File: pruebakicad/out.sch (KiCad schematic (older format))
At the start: 7 parts, among them J1 Conn_2Rows-07Pins_MountingPin, J2 Conn_01x04_MountingPin, J3 Conn_01x03, J4 Conn_2Rows-15Pins

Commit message: uart_added
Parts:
- added C6: 0.1uF, symbol Device:C_Small
- added J5: Conn_01x04, symbol Elementos:Conn_01x04
- renumbered R5 to R10, R6 to R11
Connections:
- net +3V3: now also C6.1, J5.1 (VCC)
- net GND: now also C6.2, J5.4 (GND)
- new net RXD0: J5.3 (RXD0)
- new net TXD0: J5.2 (TXD0)
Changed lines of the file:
@@
 $Descr A4 11693 8268
 encoding utf-8
-Sheet 2 3
+Sheet 2 4
 Title ""
 Date ""
@@
 $EndComp
 $Comp
-L Device:R_Small_US R5
+L Device:R_Small_US R10
 U 1 1 60810B34
 P 4050 4450
-F 0 "R5" H 4118 4496 50  0000 L CNN
+F 0 "R10" H 4118 4496 50  0000 L CNN
 F 1 "10k" H 4118 4405 50  0000 L CNN
 F 2 "" H 4050 4450 50  0001 C CNN
@@
 	4050 4700 4050 4800
 $Comp
-L Device:R_Small_US R6
+L Device:R_Small_US R11
 U 1 1 60810B54
 P 4050 4900
-F 0 "R6" H 4118 4946 50  0000 L CNN
+F 0 "R11" H 4118 4946 50  0000 L CNN
 F 1 "10k" H 4118 4855 50  0000 L CNN
 F 2 "" H 4050 4900 50  0001 C CNN
@@
 Wire Wire Line
 	6550 3650 6350 3650
+$Comp
+L Elementos:Conn_01x04 J?
+U 1 1 608DA23F
+P 7400 4750
+AR Path="/6077B277/608DA23F" Ref="J?"  Part="1"
+AR Path="/6080574C/608DA23F" Ref="J5"  Part="1"
+F 0 "J5" H 7480 4742 50  0000 L CNN
+F 1 "Conn_01x04" H 7480 4651 50  0000 L CNN
+F 2 "" H 7400 4750 50  0001 C CNN
+F 3 "~" H 7400 4750 50  0001 C CNN
+	1    7400 4750
+	1    0    0    -1
+$EndComp
+$Comp
+L Device:C_Small C?
+U 1 1 608DA247
+P 6750 4800
+AR Path="/6077B277/608DA247" Ref="C?"  Part="1"
+AR Path="/6080574C/608DA247" Ref="C6"  Part="1"
+F 0 "C6" H 6550 4850 50  0000 L CNN
+F 1 "0.1uF" H 6450 4750 50  0000 L CNN
+F 2 "" H 6750 4800 50  0001 C CNN
+F 3 "~" H 6750 4800 50  0001 C CNN
+	1    6750 4800
+	1    0    0    -1
+$EndComp
+$Comp
+L power:+3.3V #PWR?
+U 1 1 608DA251
+P 6750 4500
+AR Path="/6077B277/608DA251" Ref="#PWR?"  Part="1"
+AR Path="/6080574C/608DA251" Ref="#PWR?"  Part="1"
+F 0 "#PWR?" H 6750 4350 50  0001 C CNN
+F 1 "+3.3V" H 6765 4673 50  0000 C CNN
+F 2 "" H 6750 4500 50  0001 C CNN
+F 3 "" H 6750 4500 50  0001 C CNN
+	1    6750 4500
+	1    0    0    -1
+$EndComp
+$Comp
+L power:GND #PWR?
+U 1 1 608DA257
+P 6750 5050
+AR Path="/6077B277/608DA257" Ref="#PWR?"  Part="1"
+AR Path="/6080574C/608DA257" Ref="#PWR?"  Part="1"
+F 0 "#PWR?" H 6750 4800 50  0001 C CNN
+F 1 "GND" H 6755 4877 50  0000 C CNN
+F 2 "" H 6750 5050 50  0001 C CNN
+F 3 "" H 6750 5050 50  0001 C CNN
+	1    6750 5050
+	1    0    0    -1
+$EndComp
+Text HLabel 7100 4750 0    50   Input ~ 0
+TXD0
+Text HLabel 7100 4850 0    50   Input ~ 0
+RXD0
+Wire Wire Line
+	7200 4750 7100 4750
+Wire Wire Line
+	7200 4850 7100 4850
+Wire Wire Line
+	6750 4500 6750 4650
+Wire Wire Line
+	6750 4900 6750 4950
+Wire Wire Line
+	7200 4650 6750 4650
+Connection ~ 6750 4650
+Wire Wire Line
+	6750 4650 6750 4700
+Wire Wire Line
+	7200 4950 6750 4950
+Connection ~ 6750 4950
+Wire Wire Line
+	6750 4950 6750 5050
 $EndSCHEMATC

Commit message: footprints
Footprints added
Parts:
- BZ1: footprint (none) -> Buzzer_Beeper:Buzzer_12x9.5RM7.6
- C6: footprint (none) -> Capacitor_SMD:C_0805_2012Metric
- J1: value Conn_2Rows-07Pins_MountingPin -> Conn_01x08_RC522; footprint (none) -> Connector_PinHeader_1.00mm:PinHeader_1x08_P1.00mm_Vertical
- J2, J5: footprint (none) -> Connector_PinHeader_1.00mm:PinHeader_1x04_P1.00mm_Vertical
- J3: footprint (none) -> Connector_PinHeader_1.00mm:PinHeader_1x03_P1.00mm_Vertical
- J4: footprint (none) -> Connector_PinHeader_1.00mm:PinHeader_2x15_P1.00mm_Vertical
- R10, R11: footprint (none) -> Resistor_SMD:R_0805_2012Metric
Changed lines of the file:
@@
 $EndDescr
 $Comp
-L power:+3V3 #PWR?
+L power:+3V3 #PWR0101
 U 1 1 60810B15
 P 4300 3700
-F 0 "#PWR?" H 4300 3550 50  0001 C CNN
+F 0 "#PWR0101" H 4300 3550 50  0001 C CNN
 F 1 "+3V3" H 4315 3873 50  0000 C CNN
 F 2 "" H 4300 3700 50  0001 C CNN
@@
 $EndComp
 $Comp
-L power:GND #PWR?
+L power:GND #PWR0102
 U 1 1 60810B1D
 P 4000 3500
-F 0 "#PWR?" H 4000 3250 50  0001 C CNN
+F 0 "#PWR0102" H 4000 3250 50  0001 C CNN
 F 1 "GND" H 4005 3327 50  0000 C CNN
 F 2 "" H 4000 3500 50  0001 C CNN
@@
 	4550 4800 4300 4800
 $Comp
-L power:GND #PWR?
+L power:GND #PWR0103
 U 1 1 60810B26
 P 4300 4950
-F 0 "#PWR?" H 4300 4700 50  0001 C CNN
+F 0 "#PWR0103" H 4300 4700 50  0001 C CNN
 F 1 "GND" H 4305 4777 50  0000 C CNN
 F 2 "" H 4300 4950 50  0001 C CNN
@@
 	4300 4800 4300 4950
 $Comp
-L power:+5V #PWR?
+L power:+5V #PWR0104
 U 1 1 60810B2E
 P 4300 4400
-F 0 "#PWR?" H 4300 4250 50  0001 C CNN
+F 0 "#PWR0104" H 4300 4250 50  0001 C CNN
 F 1 "+5V" H 4315 4573 50  0000 C CNN
 F 2 "" H 4300 4400 50  0001 C CNN
@@
 F 0 "R10" H 4118 4496 50  0000 L CNN
 F 1 "10k" H 4118 4405 50  0000 L CNN
-F 2 "" H 4050 4450 50  0001 C CNN
+F 2 "Resistor_SMD:R_0805_2012Metric" H 4050 4450 50  0001 C CNN
 F 3 "~" H 4050 4450 50  0001 C CNN
 	1    4050 4450
@@
 	4050 4350 4050 4250
 $Comp
-L power:+5V #PWR?
+L power:+5V #PWR0105
 U 1 1 60810B3F
 P 4050 4250
-F 0 "#PWR?" H 4050 4100 50  0001 C CNN
+F 0 "#PWR0105" H 4050 4100 50  0001 C CNN
 F 1 "+5V" H 4065 4423 50  0000 C CNN
 F 2 "" H 4050 4250 50  0001 C CNN
@@
 F 0 "J2" H 4838 4514 50  0000 L CNN
 F 1 "Conn_01x04_MountingPin" H 4838 4423 50  0000 L CNN
-F 2 "" H 4750 4600 50  0001 C CNN
+F 2 "Connector_PinHeader_1.00mm:PinHeader_1x04_P1.00mm_Vertical" H 4750 4600 50  0001 C CNN
 F 3 "~" H 4750 4600 50  0001 C CNN
 	1    4750 4600
@@
 $EndComp
 $Comp
-L power:+5V #PWR?
+L power:+5V #PWR0106
 U 1 1 60810B4B
 P 4050 5100
-F 0 "#PWR?" H 4050 4950 50  0001 C CNN
+F 0 "#PWR0106" H 4050 4950 50  0001 C CNN
 F 1 "+5V" H 4065 5273 50  0000 C CNN
 F 2 "" H 4050 5100 50  0001 C CNN
@@
 F 0 "R11" H 4118 4946 50  0000 L CNN
 F 1 "10k" H 4118 4855 50  0000 L CNN
-F 2 "" H 4050 4900 50  0001 C CNN
+F 2 "Resistor_SMD:R_0805_2012Metric" H 4050 4900 50  0001 C CNN
 F 3 "~" H 4050 4900 50  0001 C CNN
 	1    4050 4900
@@
 F 0 "BZ1" H 4702 2279 50  0000 L CNN
 F 1 "Buzzer" H 4702 2188 50  0000 L CNN
-F 2 "" V 4525 2350 50  0001 C CNN
+F 2 "Buzzer_Beeper:Buzzer_12x9.5RM7.6" V 4525 2350 50  0001 C CNN
 F 3 "~" V 4525 2350 50  0001 C CNN
 	1    4550 2250
@@
 $EndComp
 $Comp
-L power:GND #PWR?
+L power:GND #PWR0107
 U 1 1 60810B6A
 P 4450 2500
-F 0 "#PWR?" H 4450 2250 50  0001 C CNN
+F 0 "#PWR0107" H 4450 2250 50  0001 C CNN
 F 1 "GND" H 4455 2327 50  0000 C CNN
 F 2 "" H 4450 2500 50  0001 C CNN
@@
 F 0 "J3" H 4830 5642 50  0000 L CNN
 F 1 "Conn_01x03" H 4830 5551 50  0000 L CNN
-F 2 "" H 4750 5600 50  0001 C CNN
+F 2 "Connector_PinHeader_1.00mm:PinHeader_1x03_P1.00mm_Vertical" H 4750 5600 50  0001 C CNN
 F 3 "~" H 4750 5600 50  0001 C CNN
 	1    4750 5600
@@
 	4550 5700 4350 5700
 $Comp
-L power:GND #PWR?
+L power:GND #PWR0108
 U 1 1 60810B7C
 P 4150 5650
-F 0 "#PWR?" H 4150 5400 50  0001 C CNN
+F 0 "#PWR0108" H 4150 5400 50  0001 C CNN
 F 1 "GND" H 4155 5477 50  0000 C CNN
 F 2 "" H 4150 5650 50  0001 C CNN
@@
 $EndComp
 $Comp
-L power:+5V #PWR?
+L power:+5V #PWR0109
 U 1 1 60810B82
 P 4350 5800
-F 0 "#PWR?" H 4350 5650 50  0001 C CNN
+F 0 "#PWR0109" H 4350 5650 50  0001 C CNN
 F 1 "+5V" H 4365 5973 50  0000 C CNN
 F 2 "" H 4350 5800 50  0001 C CNN
@@
 AR Path="/6080574C/60810B0A" Ref="J1"  Part="1"
 F 0 "J1" H 4750 3800 50  0000 C CNN
-F 1 "Conn_2Rows-07Pins_MountingPin" H 4750 3700 50  0000 C CNN
-F 2 "" H 4750 3300 50  0001 C CNN
+F 1 "Conn_01x08_RC522" H 4750 3700 50  0000 C CNN
+F 2 "Connector_PinHeader_1.00mm:PinHeader_1x08_P1.00mm_Vertical" H 4750 3300 50  0001 C CNN
 F 3 "~" H 4750 3300 50  0001 C CNN
 	1    4750 3300
@@
 F 0 "J4" H 6850 3967 50  0000 C CNN
 F 1 "Conn_2Rows-15Pins" H 6850 3876 50  0000 C CNN
-F 2 "" H 6800 3350 50  0001 C CNN
+F 2 "Connector_PinHeader_1.00mm:PinHeader_2x15_P1.00mm_Vertical" H 6800 3350 50  0001 C CNN
 F 3 "~" H 6800 3350 50  0001 C CNN
 	1    6800 3350
@@
 	6350 3650 6350 3700
 $Comp
-L power:GND #PWR?
+L power:GND #PWR0110
 U 1 1 60833C66
 P 6350 3700
-F 0 "#PWR?" H 6350 3450 50  0001 C CNN
+F 0 "#PWR0110" H 6350 3450 50  0001 C CNN
 F 1 "GND" H 6355 3527 50  0000 C CNN
 F 2 "" H 6350 3700 50  0001 C CNN
@@
 $EndComp
 $Comp
-L power:+3.3V #PWR?
+L power:+3.3V #PWR0111
 U 1 1 608343FF
 P 6350 2850
-F 0 "#PWR?" H 6350 2700 50  0001 C CNN
+F 0 "#PWR0111" H 6350 2700 50  0001 C CNN
 F 1 "+3.3V" H 6365 3023 50  0000 C CNN
 F 2 "" H 6350 2850 50  0001 C CNN
@@
 	7100 3650 7300 3650
 $Comp
-L power:+5V #PWR?
+L power:+5V #PWR0112
 U 1 1 6083FA93
 P 7300 3650
-F 0 "#PWR?" H 7300 3500 50  0001 C CNN
+F 0 "#PWR0112" H 7300 3500 50  0001 C CNN
 F 1 "+5V" H 7315 3823 50  0000 C CNN
 F 2 "" H 7300 3650 50  0001 C CNN
@@
 F 0 "J5" H 7480 4742 50  0000 L CNN
 F 1 "Conn_01x04" H 7480 4651 50  0000 L CNN
-F 2 "" H 7400 4750 50  0001 C CNN
+F 2 "Connector_PinHeader_1.00mm:PinHeader_1x04_P1.00mm_Vertical" H 7400 4750 50  0001 C CNN
 F 3 "~" H 7400 4750 50  0001 C CNN
 	1    7400 4750
@@
 F 0 "C6" H 6550 4850 50  0000 L CNN
 F 1 "0.1uF" H 6450 4750 50  0000 L CNN
-F 2 "" H 6750 4800 50  0001 C CNN
+F 2 "Capacitor_SMD:C_0805_2012Metric" H 6750 4800 50  0001 C CNN
 F 3 "~" H 6750 4800 50  0001 C CNN
 	1    6750 4800
@@
 P 6750 4500
 AR Path="/6077B277/608DA251" Ref="#PWR?"  Part="1"
-AR Path="/6080574C/608DA251" Ref="#PWR?"  Part="1"
-F 0 "#PWR?" H 6750 4350 50  0001 C CNN
+AR Path="/6080574C/608DA251" Ref="#PWR0113"  Part="1"
+F 0 "#PWR0113" H 6750 4350 50  0001 C CNN
 F 1 "+3.3V" H 6765 4673 50  0000 C CNN
 F 2 "" H 6750 4500 50  0001 C CNN
@@
 P 6750 5050
 AR Path="/6077B277/608DA257" Ref="#PWR?"  Part="1"
-AR Path="/6080574C/608DA257" Ref="#PWR?"  Part="1"
-F 0 "#PWR?" H 6750 4800 50  0001 C CNN
+AR Path="/6080574C/608DA257" Ref="#PWR0114"  Part="1"
+F 0 "#PWR0114" H 6750 4800 50  0001 C CNN
 F 1 "GND" H 6755 4877 50  0000 C CNN
 F 2 "" H 6750 5050 50  0001 C CNN

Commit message: pcb1.0
created pcb
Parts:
- J4: footprint Connector_PinHeader_1.00mm:PinHeader_2x15_P1.00mm_Vertical -> Connector_PinHeader_1.00mm:PinHeader_2x09_P1.00mm_Vertical
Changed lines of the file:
@@
 U 1 1 60810B73
 P 4750 5600
+AR Path="/60810B73" Ref="J3"  Part="1"
+AR Path="/6080574C/60810B73" Ref="J3"  Part="1"
 F 0 "J3" H 4830 5642 50  0000 L CNN
 F 1 "Conn_01x03" H 4830 5551 50  0000 L CNN
@@
 F 0 "J4" H 6850 3967 50  0000 C CNN
 F 1 "Conn_2Rows-15Pins" H 6850 3876 50  0000 C CNN
-F 2 "Connector_PinHeader_1.00mm:PinHeader_2x15_P1.00mm_Vertical" H 6800 3350 50  0001 C CNN
+F 2 "Connector_PinHeader_1.00mm:PinHeader_2x09_P1.00mm_Vertical" H 6800 3350 50  0001 C CNN
 F 3 "~" H 6800 3350 50  0001 C CNN
 	1    6800 3350

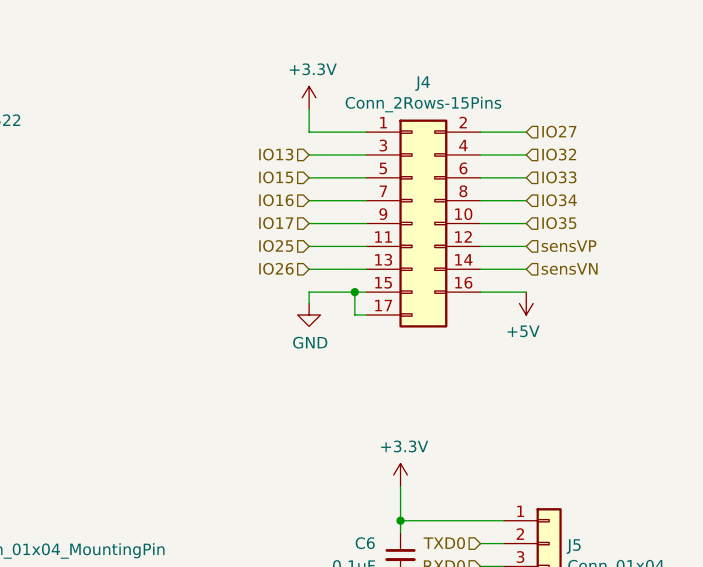
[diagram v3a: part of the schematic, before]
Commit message: wires updated
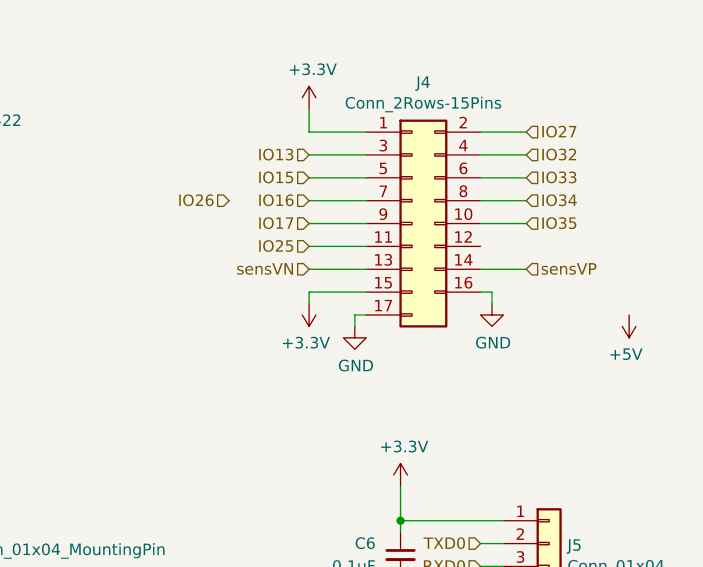
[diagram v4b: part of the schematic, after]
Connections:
- net +3V3: now also J4.15 (GND)
- net +5V: no longer J4.16 (5V)
- net GND: now also J4.16 (5V); no longer J4.15 (GND)
- net IO26: no longer J4.13 (IO26)
- net sensVN: now also J4.13 (IO26); no longer J4.14 (sensVN)
- net sensVP: now also J4.14 (sensVN); no longer J4.12 (sensVP)
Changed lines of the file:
@@
 Wire Wire Line
 	6350 2950 6350 2850
-Wire Wire Line
-	6600 3650 6550 3650
-Wire Wire Line
-	6350 3650 6350 3700
 $Comp
 L power:GND #PWR0110
 U 1 1 60833C66
-P 6350 3700
-F 0 "#PWR0110" H 6350 3450 50  0001 C CNN
-F 1 "GND" H 6355 3527 50  0000 C CNN
-F 2 "" H 6350 3700 50  0001 C CNN
-F 3 "" H 6350 3700 50  0001 C CNN
-	1    6350 3700
+P 6550 3800
+F 0 "#PWR0110" H 6550 3550 50  0001 C CNN
+F 1 "GND" H 6555 3627 50  0000 C CNN
+F 2 "" H 6550 3800 50  0001 C CNN
+F 3 "" H 6550 3800 50  0001 C CNN
+	1    6550 3800
 	1    0    0    -1
 $EndComp
@@
 	6350 3450 6600 3450
 Wire Wire Line
-	6600 3550 6350 3550
-Wire Wire Line
 	7100 2950 7300 2950
 Wire Wire Line
@@
 Wire Wire Line
 	7100 3350 7300 3350
-Wire Wire Line
-	7100 3450 7300 3450
-Wire Wire Line
-	7100 3550 7300 3550
 Text HLabel 6350 3050 0    50   Input ~ 0
 IO13
@@
 Text HLabel 6350 3450 0    50   Input ~ 0
 IO25
-Text HLabel 6350 3550 0    50   Input ~ 0
+Text HLabel 6000 3250 0    50   Input ~ 0
 IO26
 Text HLabel 7300 2950 2    50   Input ~ 0
@@
 Text HLabel 7300 3350 2    50   Input ~ 0
 IO35
-Text HLabel 7300 3450 2    50   Input ~ 0
+Text HLabel 7300 3550 2    50   Input ~ 0
 sensVP
-Text HLabel 7300 3550 2    50   Input ~ 0
+Text HLabel 6350 3550 0    50   Input ~ 0
 sensVN
-Wire Wire Line
-	7100 3650 7300 3650
 $Comp
 L power:+5V #PWR0112
 U 1 1 6083FA93
-P 7300 3650
-F 0 "#PWR0112" H 7300 3500 50  0001 C CNN
-F 1 "+5V" H 7315 3823 50  0000 C CNN
-F 2 "" H 7300 3650 50  0001 C CNN
-F 3 "" H 7300 3650 50  0001 C CNN
-	1    7300 3650
+P 7750 3750
+F 0 "#PWR0112" H 7750 3600 50  0001 C CNN
+F 1 "+5V" H 7765 3923 50  0000 C CNN
+F 2 "" H 7750 3750 50  0001 C CNN
+F 3 "" H 7750 3750 50  0001 C CNN
+	1    7750 3750
 	-1   0    0    1
 $EndComp
 Wire Wire Line
 	6600 3750 6550 3750
-Wire Wire Line
-	6550 3750 6550 3650
-Connection ~ 6550 3650
-Wire Wire Line
-	6550 3650 6350 3650
 $Comp
 L Elementos:Conn_01x04 J?
@@
 Wire Wire Line
 	6750 4950 6750 5050
+Wire Wire Line
+	6550 3800 6550 3750
+$Comp
+L power:GND #PWR0139
+U 1 1 60DE4342
+P 7150 3700
+F 0 "#PWR0139" H 7150 3450 50  0001 C CNN
+F 1 "GND" H 7155 3527 50  0000 C CNN
+F 2 "" H 7150 3700 50  0001 C CNN
+F 3 "" H 7150 3700 50  0001 C CNN
+	1    7150 3700
+	1    0    0    -1
+$EndComp
+Wire Wire Line
+	7150 3700 7150 3650
+Wire Wire Line
+	7150 3650 7100 3650
+$Comp
+L power:+3.3V #PWR0140
+U 1 1 60DE61D5
+P 6350 3700
+F 0 "#PWR0140" H 6350 3550 50  0001 C CNN
+F 1 "+3.3V" H 6365 3873 50  0000 C CNN
+F 2 "" H 6350 3700 50  0001 C CNN
+F 3 "" H 6350 3700 50  0001 C CNN
+	1    6350 3700
+	-1   0    0    1
+$EndComp
+Wire Wire Line
+	6600 3650 6350 3650
+Wire Wire Line
+	6350 3650 6350 3700
+Wire Wire Line
+	6600 3550 6350 3550
+Wire Wire Line
+	7300 3550 7100 3550
 $EndSCHEMATC

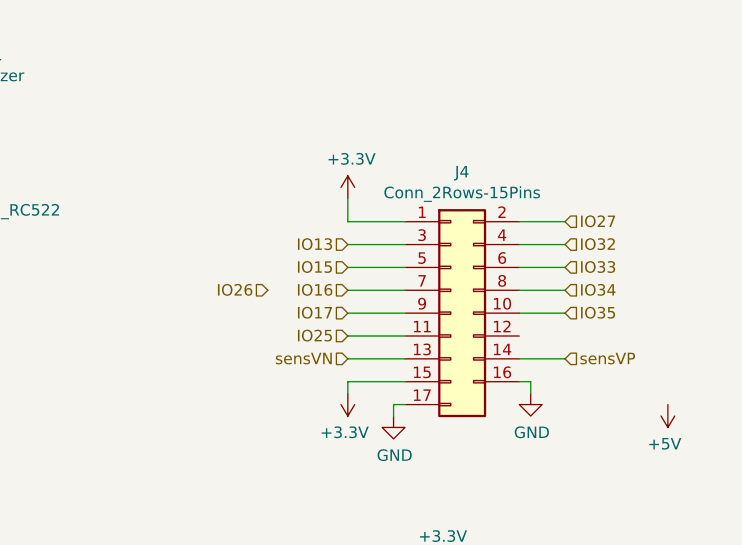
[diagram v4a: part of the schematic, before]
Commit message: wires updated
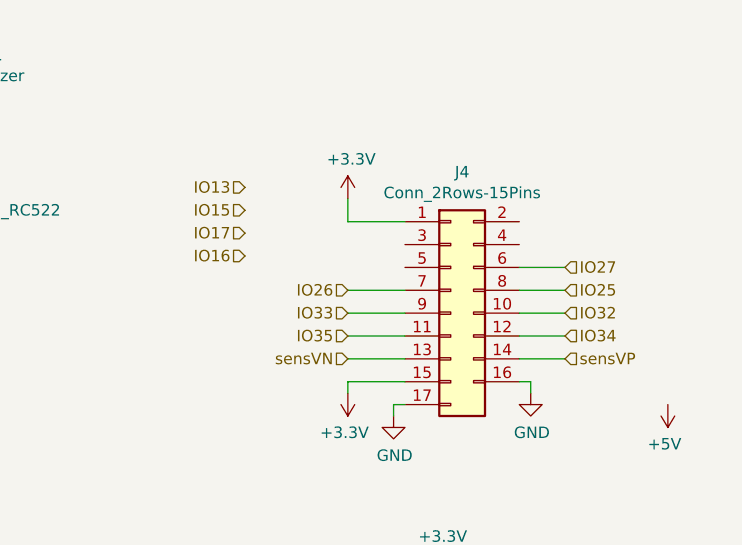
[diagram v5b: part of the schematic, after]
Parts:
- J4: footprint Connector_PinHeader_1.00mm:PinHeader_2x09_P1.00mm_Vertical -> Connector_PinSocket_2.54mm:PinSocket_2x09_P2.54mm_Vertical
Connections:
- net IO13: no longer J4.3 (IO13)
- net IO15: no longer J4.5 (IO15)
- net IO16: no longer J4.7 (IO16)
- net IO17: no longer J4.9 (IO17)
- net IO25: now also J4.8 (IO34); no longer J4.11 (IO25)
- net IO26: now also J4.7 (IO16)
- net IO27: now also J4.6 (IO33); no longer J4.2 (IO27)
- net IO32: now also J4.10 (IO35); no longer J4.4 (IO32)
- net IO33: now also J4.9 (IO17); no longer J4.6 (IO33)
- net IO34: now also J4.12 (sensVP); no longer J4.8 (IO34)
- net IO35: now also J4.11 (IO25); no longer J4.10 (IO35)
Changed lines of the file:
@@
 F 0 "J4" H 6850 3967 50  0000 C CNN
 F 1 "Conn_2Rows-15Pins" H 6850 3876 50  0000 C CNN
-F 2 "Connector_PinHeader_1.00mm:PinHeader_2x09_P1.00mm_Vertical" H 6800 3350 50  0001 C CNN
+F 2 "Connector_PinSocket_2.54mm:PinSocket_2x09_P2.54mm_Vertical" H 6800 3350 50  0001 C CNN
 F 3 "~" H 6800 3350 50  0001 C CNN
 	1    6800 3350
@@
 	1    0    0    -1
 $EndComp
-Wire Wire Line
-	6600 3050 6350 3050
-Wire Wire Line
-	6600 3150 6350 3150
-Wire Wire Line
-	6600 3250 6350 3250
-Wire Wire Line
-	6600 3350 6350 3350
-Wire Wire Line
-	6350 3450 6600 3450
-Wire Wire Line
-	7100 2950 7300 2950
-Wire Wire Line
-	7100 3050 7300 3050
-Wire Wire Line
-	7100 3150 7300 3150
-Wire Wire Line
-	7100 3250 7300 3250
-Wire Wire Line
-	7100 3350 7300 3350
-Text HLabel 6350 3050 0    50   Input ~ 0
+Text HLabel 5900 2800 0    50   Input ~ 0
 IO13
-Text HLabel 6350 3150 0    50   Input ~ 0
+Text HLabel 5900 2900 0    50   Input ~ 0
 IO15
+Text HLabel 5900 3100 0    50   Input ~ 0
+IO16
+Text HLabel 5900 3000 0    50   Input ~ 0
+IO17
+Text HLabel 7300 3250 2    50   Input ~ 0
+IO25
 Text HLabel 6350 3250 0    50   Input ~ 0
-IO16
+IO26
+Text HLabel 7300 3150 2    50   Input ~ 0
+IO27
+Text HLabel 7300 3350 2    50   Input ~ 0
+IO32
 Text HLabel 6350 3350 0    50   Input ~ 0
-IO17
+IO33
+Text HLabel 7300 3450 2    50   Input ~ 0
+IO34
 Text HLabel 6350 3450 0    50   Input ~ 0
-IO25
-Text HLabel 6000 3250 0    50   Input ~ 0
-IO26
-Text HLabel 7300 2950 2    50   Input ~ 0
-IO27
-Text HLabel 7300 3050 2    50   Input ~ 0
-IO32
-Text HLabel 7300 3150 2    50   Input ~ 0
-IO33
-Text HLabel 7300 3250 2    50   Input ~ 0
-IO34
-Text HLabel 7300 3350 2    50   Input ~ 0
 IO35
 Text HLabel 7300 3550 2    50   Input ~ 0
@@
 Wire Wire Line
 	7300 3550 7100 3550
+Wire Wire Line
+	7100 3450 7300 3450
+Wire Wire Line
+	6600 3450 6350 3450
+Wire Wire Line
+	7300 3350 7100 3350
+Wire Wire Line
+	6600 3350 6350 3350
+Wire Wire Line
+	7300 3250 7100 3250
+Wire Wire Line
+	6600 3250 6350 3250
+Wire Wire Line
+	7300 3150 7100 3150
 $EndSCHEMATC
